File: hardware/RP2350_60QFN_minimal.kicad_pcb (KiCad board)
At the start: 2 copper layers, 139 parts, among them J1 UJ20-C-H-G-SMT-2A-P16-TR, J2 73101-0570, J3 73101-0570, J4 PinHeader_1x03, J5 4677, SW1 SW_Push, SW2 SW_Push, U1 RP2350_60QFN, U10 ADG621BRMZ, U13 TLP3441TP_F, U15 ADG621BRMZ, U2 REF35330QDBVR, U3 W25Q128JVS, U4 LM27762, U5 NCP1117-3.3_SOT223, U6 MCP47FEB02A0T-E/ST, U7 Opamp_Dual, U8 TLP3441TP_F, Y1 ABM8-272-T3

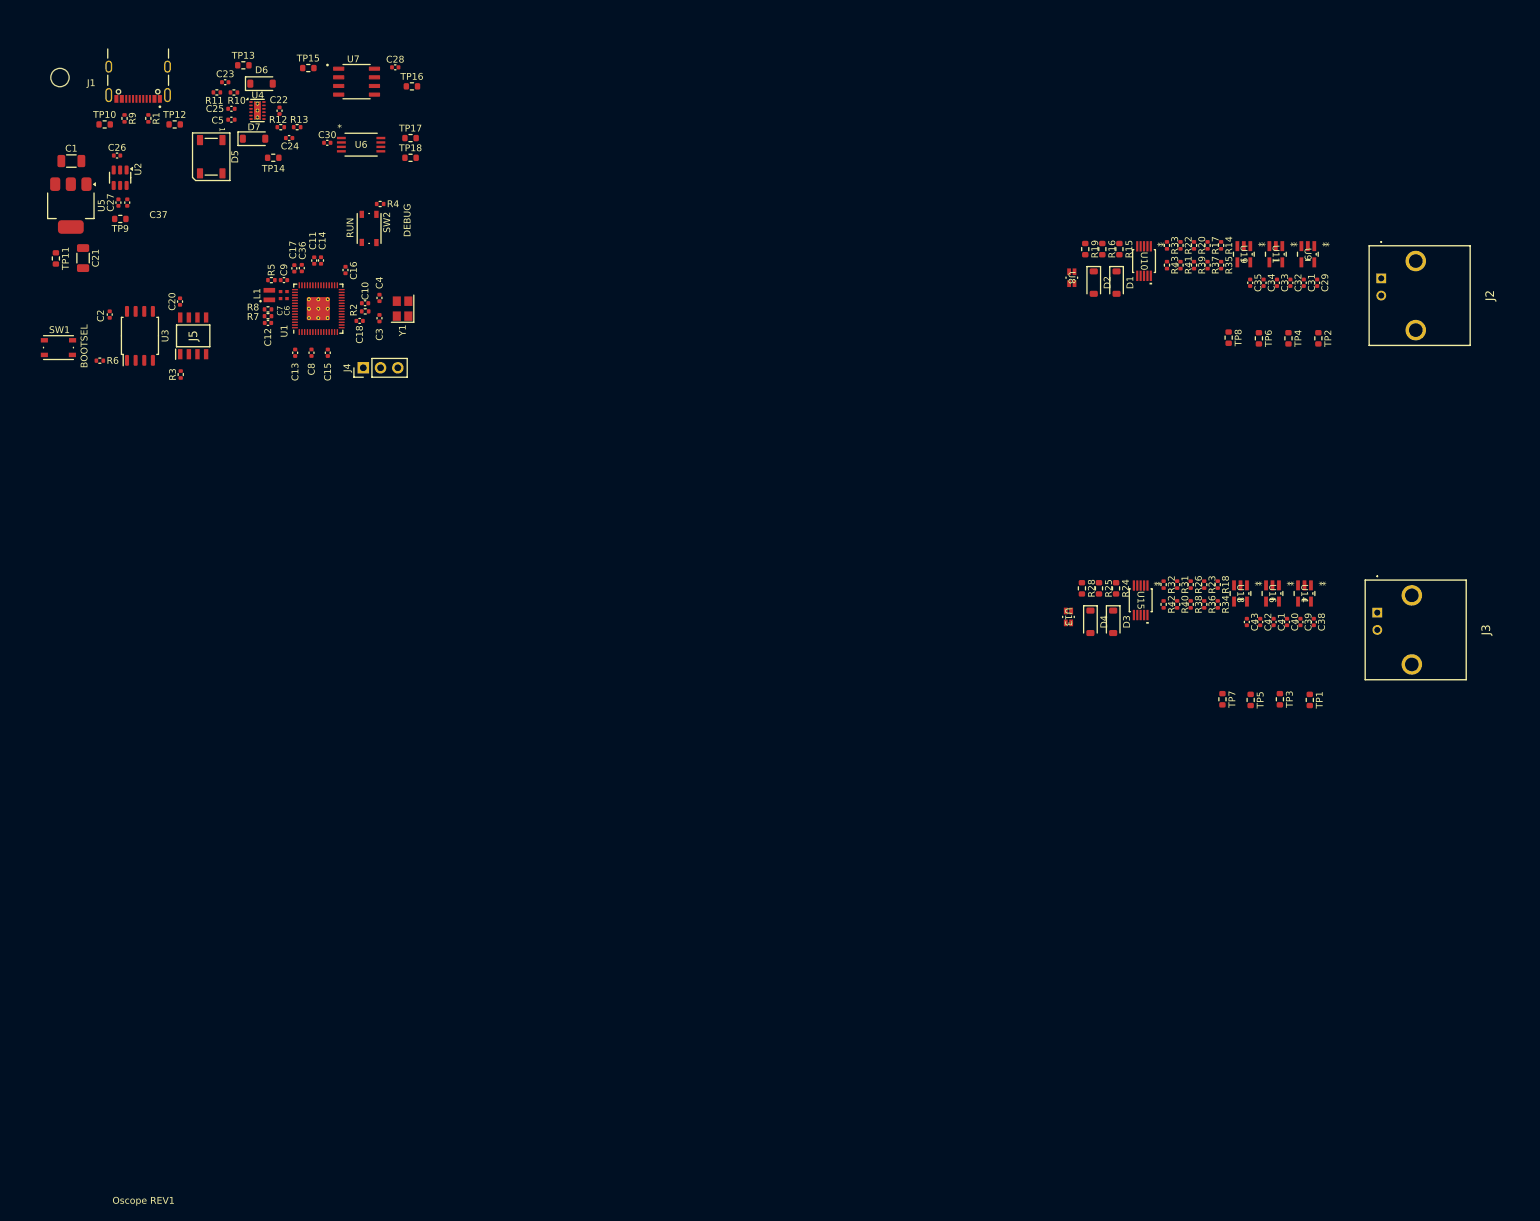
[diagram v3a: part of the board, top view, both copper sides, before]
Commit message: feat(hardware): Fix disconnected analog block pins
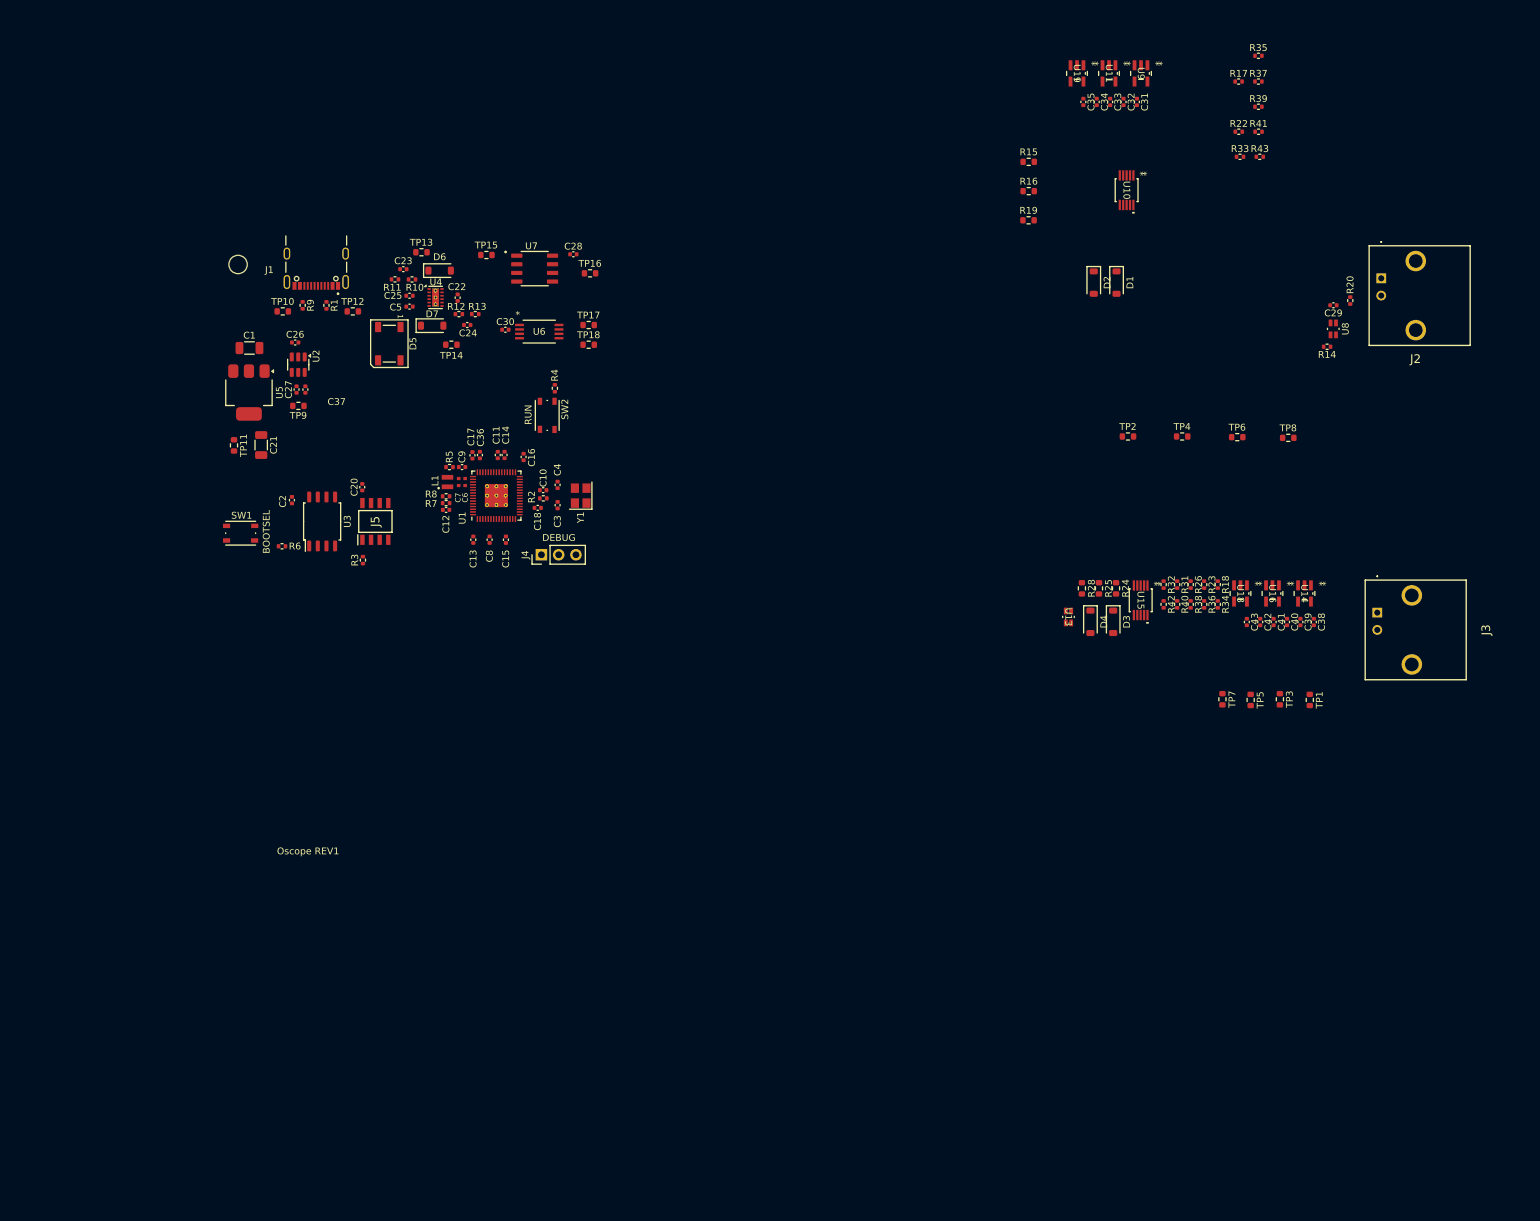
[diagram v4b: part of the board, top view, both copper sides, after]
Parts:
- moved C14 39.3 mm to (97.9, 77.9)
- moved C11 39.3 mm to (96.9, 77.9)
- moved U8 39.2 mm to (219.8, 59.4), turned to 90 degrees
- moved C20 38.3 mm to (77.0, 82.7)
- moved R3 38.3 mm to (77.1, 93.4)
- moved C2 38.3 mm to (66.6, 84.6)
- moved J5 38.3 mm to (78.9, 87.7)
- moved R6 38.3 mm to (65.2, 91.3)
- moved SW1 38.3 mm to (59.1, 89.4)
- moved U3 38.3 mm to (71.1, 87.7)
- moved C13 38.0 mm to (93.3, 90.4)
- moved C36 38.0 mm to (94.3, 77.9)
- moved C7 38.0 mm to (91.2, 81.9)
- moved L1 38.0 mm to (89.5, 81.9)
- moved TP11 38.0 mm to (58.1, 76.5)
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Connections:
- R14 pad 1: unconnected-(R14-Pad1) -> Net-(R14-Pad1)
- R23 pad 1: unconnected-(R23-Pad1) -> Net-(R23-Pad1)
- U13 pad 1: unconnected-(U13-Pad1) -> Net-(R23-Pad1)
- U13 pad 2: unconnected-(U13-Pad2) -> GNDA
- U13 pad 4: unconnected-(U13-Pad4) -> Net-(C38-Pad2)
- U8 pad 1: unconnected-(U8-Pad1) -> Net-(R14-Pad1)
- U8 pad 2: unconnected-(U8-Pad2) -> GNDA
- U8 pad 4: unconnected-(U8-Pad4) -> Net-(C29-Pad2)

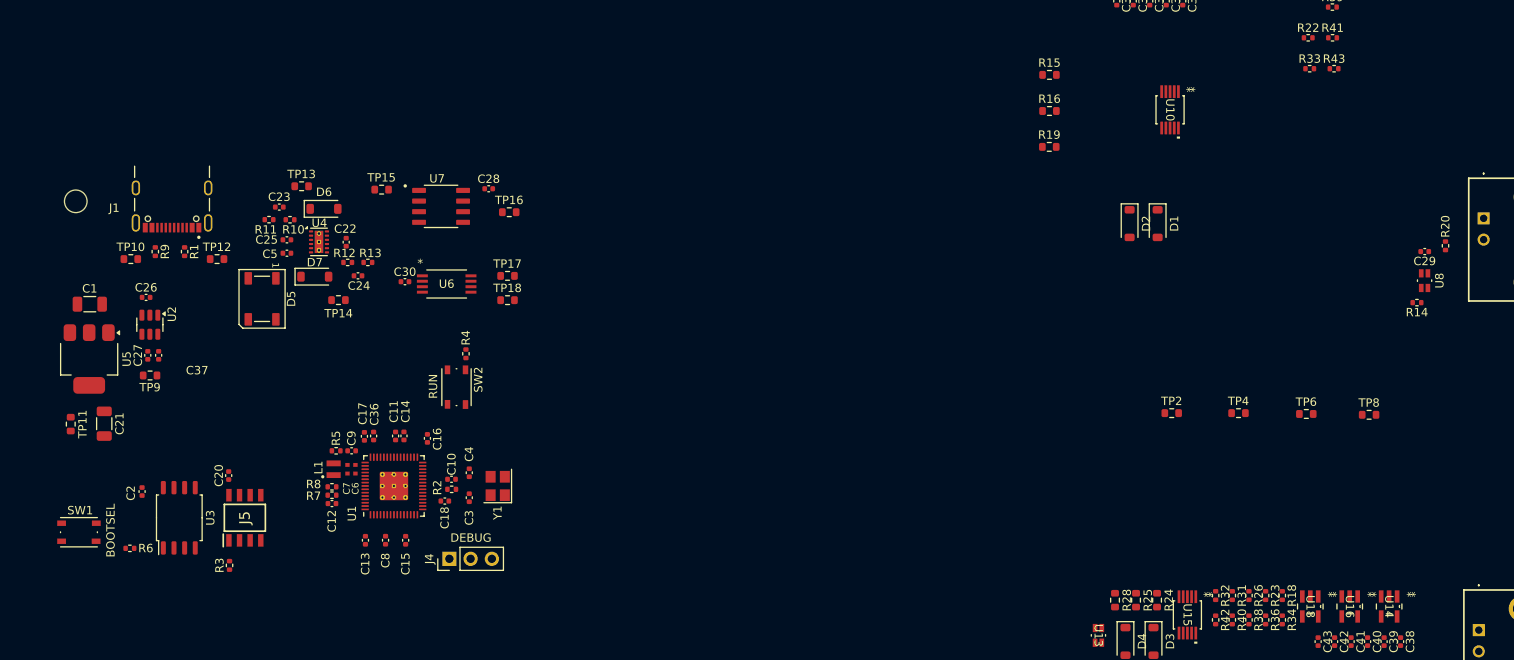
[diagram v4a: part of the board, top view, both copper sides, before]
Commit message: feat(hardware): Update switch footprint
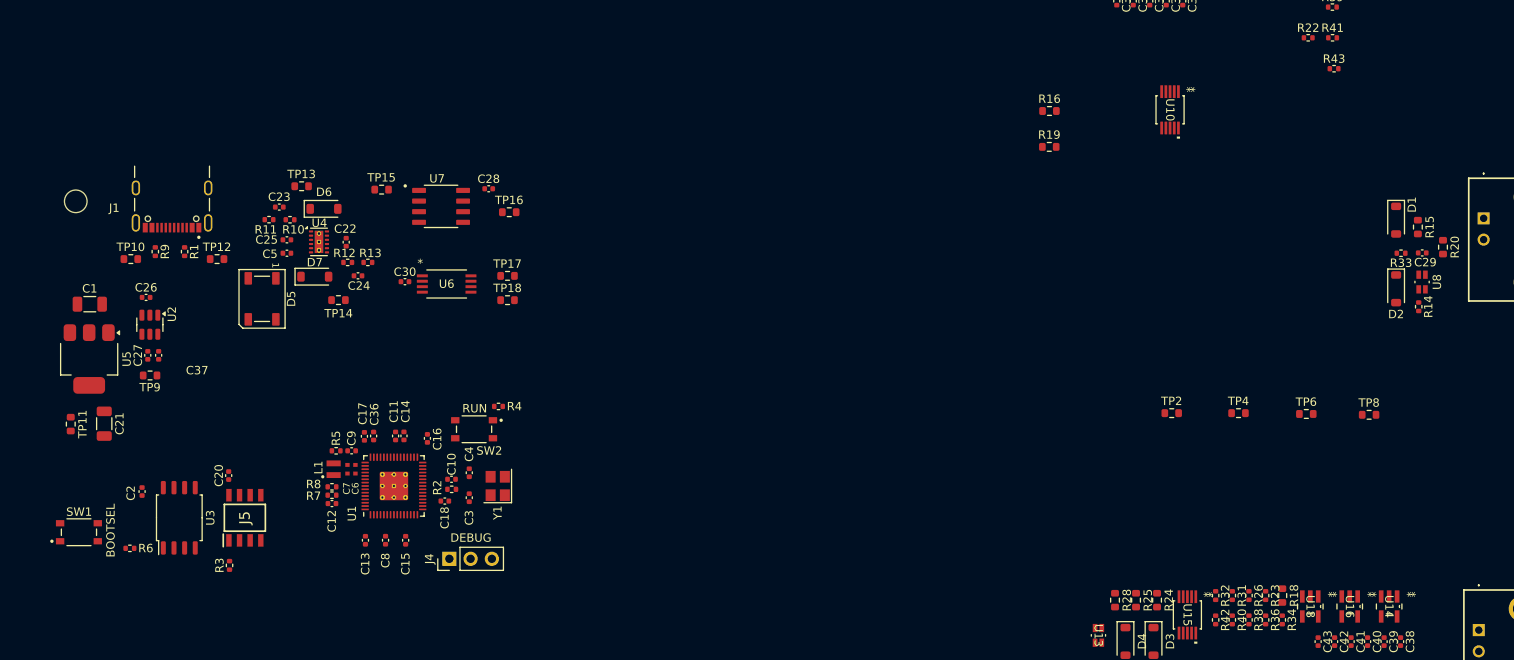
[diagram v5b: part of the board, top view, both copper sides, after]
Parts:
- R18, R20: footprint Resistor_SMD:R_0402_1005Metric -> Resistor_SMD:R_0603_1608Metric
- SW1, SW2: footprint Button_Switch_SMD:SW_Push_1P1T_NO_Vertical_Wuerth_434133025816 -> TL3365AF180QG:SW_TL3365AF180QG
- moved R15 47.6 mm to (219.0, 53.0), turned to -90 degrees
- moved D2 32.8 mm to (216.4, 60.4)
- moved D1 28.5 mm to (216.4, 52.1)
- moved R33 24.6 mm to (217.0, 56.1), turned to 180 degrees
- moved R4 7.40 mm to (109.2, 74.4), turned to 0 degrees
- moved SW2 5.45 mm to (106.3, 77.1), turned to 180 degrees
- moved R14 0.53 mm to (219.1, 62.5), turned to -90 degrees
- moved R20 0.34 mm to (222.0, 55.4)
- moved U8 0.34 mm to (219.5, 59.5)
- moved C29 0.34 mm to (219.5, 56.1)

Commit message: feat(hardware): Layout analog block 1
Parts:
- moved R19 41.8 mm to (213.0, 60.7), turned to 90 degrees
- moved C33 38.9 mm to (210.4, 57.1), turned to 180 degrees
- moved R37 38.2 mm to (200.7, 60.3), turned to 90 degrees
- moved U9 36.8 mm to (212.4, 52.2), turned to 180 degrees
- moved U11 35.9 mm to (205.9, 52.2), turned to 180 degrees
- moved R16 35.2 mm to (203.4, 59.9), turned to 90 degrees
- moved R35 34.6 mm to (202.2, 53.2), turned to 180 degrees
- moved U19 34.5 mm to (198.5, 52.2), turned to 180 degrees
- moved R17 32.1 mm to (205.9, 55.1), turned to 180 degrees
- moved C31 31.7 mm to (212.4, 49.3), turned to 180 degrees
- moved R39 30.9 mm to (201.7, 56.8), turned to 180 degrees
- moved C32 28.8 mm to (205.9, 49.3), turned to 180 degrees
- moved U10 28.2 mm to (208.3, 59.9), turned to 0 degrees
- moved C35 27.7 mm to (194.3, 51.3), turned to 90 degrees
- moved C34 26.9 mm to (198.5, 49.3), turned to 180 degrees
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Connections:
- R17 pad 1: Net-(U10-NC) -> Net-(U10-S1)
- R26 pad 1: Net-(U15-NC) -> Net-(U15-S1)
- U10 pad 1: Net-(U10-NC) -> Net-(U10-S1)
- U10 pad 6: Net-(U10-NC) -> unconnected-(U10-NC-Pad6)
- U10 pad 7: Net-(U10-NC) -> Net-(U10-S1)
- U11 pad 2: Net-(U10-NC) -> Net-(U10-S1)
- U15 pad 1: Net-(U15-NC) -> Net-(U15-S1)
- U15 pad 6: Net-(U15-NC) -> unconnected-(U15-NC-Pad6)
- U15 pad 7: Net-(U15-NC) -> Net-(U15-S1)
- U16 pad 2: Net-(U15-NC) -> Net-(U15-S1)

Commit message: feat(hardware): Finish component layout
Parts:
- removed H4: MountingHole, MountingHole:MountingHole_2.7mm_M2.5
- moved H3 178.6 mm to (114.9, 85.1)
- moved H2 144.6 mm to (143.4, 67.0)
- moved TP1 104.9 mm to (116.9, 80.5)
- moved C43 94.6 mm to (116.7, 74.6), turned to 90 degrees
- moved C42 93.1 mm to (120.9, 72.6), turned to 180 degrees
- moved C40 89.8 mm to (128.3, 72.6), turned to 180 degrees
- moved U18 88.3 mm to (120.9, 75.5), turned to 180 degrees
- moved U16 85.7 mm to (128.3, 75.5), turned to 180 degrees
- moved C39 85.5 mm to (134.8, 72.6), turned to 180 degrees
- moved U14 83.9 mm to (134.8, 75.5), turned to 180 degrees
- moved R31 82.3 mm to (117.2, 76.4), turned to 180 degrees
- moved R34 81.6 mm to (124.6, 76.5), turned to 180 degrees
- moved C19 81.5 mm to (86.3, 86.1)
- moved C41 81.3 mm to (132.8, 80.4), turned to 180 degrees
- moved J3 81.3 mm to (149.3, 75.2)
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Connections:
- C28 pad 2: GND -> GNDA
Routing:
- net /CHB_SELC: track 0.00 -> 5.03 mm
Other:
- board outline added: 106.9 x 43.5 mm

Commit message: feat(hardware): updted design rules
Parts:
- removed NT1, NT2: NetTie_2, NetTie:NetTie-2_SMD_Pad0.5mm
- added FB1: FerriteBead, Resistor_SMD:R_0603_1608Metric, F.Cu at (136.9, 105.2)
- moved H3 65.2 mm to (156.0, 135.7)
- moved H2 63.5 mm to (183.0, 116.7)
- moved C24 63.2 mm to (131.6, 108.3)
- moved C33 63.2 mm to (172.0, 108.5)
- moved J3 63.2 mm to (188.5, 124.8)
- moved R14 63.2 mm to (180.7, 111.9)
- moved R15 63.2 mm to (180.6, 102.4)
- moved R19 63.2 mm to (174.6, 112.2)
- moved R26 63.2 mm to (167.5, 127.9)
- moved R32 63.2 mm to (178.6, 126.9)
- moved TP16 63.2 mm to (149.7, 100.7)
- moved TP6 63.2 mm to (171.3, 115.7)
- moved U14 63.2 mm to (174.0, 125.0)
- moved U16 63.2 mm to (167.5, 125.0)
- moved U8 63.2 mm to (181.1, 109.0)
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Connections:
- C28 pad 2: GNDA -> GND
- C33 pad 2: GNDA -> GND
- C34 pad 2: GNDA -> GND
- C35 pad 2: GNDA -> GND
- C41 pad 2: GNDA -> GND
- C42 pad 2: GNDA -> GND
- C43 pad 2: GNDA -> GND
- J2 pad 1: GNDA -> GND
- J3 pad 1: GNDA -> GND
- R15 pad 1: GNDA -> GND
- R16 pad 1: GNDA -> GND
- R19 pad 1: GNDA -> GND
- R24 pad 1: GNDA -> GND
- R25 pad 1: GNDA -> GND
- R28 pad 1: GNDA -> GND
- R38 pad 2: GNDA -> GND
- R39 pad 2: GNDA -> GND
- R42 pad 2: GNDA -> GND
- R43 pad 2: GNDA -> GND
- U10 pad 4: GNDA -> GND
- U13 pad 2: GNDA -> GND
- U15 pad 4: GNDA -> GND
- U18 pad 4: GNDA -> GND
- U19 pad 4: GNDA -> GND
- U7 pad 4: GNDA -> GND
- U8 pad 2: GNDA -> GND
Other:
- copper layers 2 -> 4
